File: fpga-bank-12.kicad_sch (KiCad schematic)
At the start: 1 part, among them U4 XC7K160T-FFG676

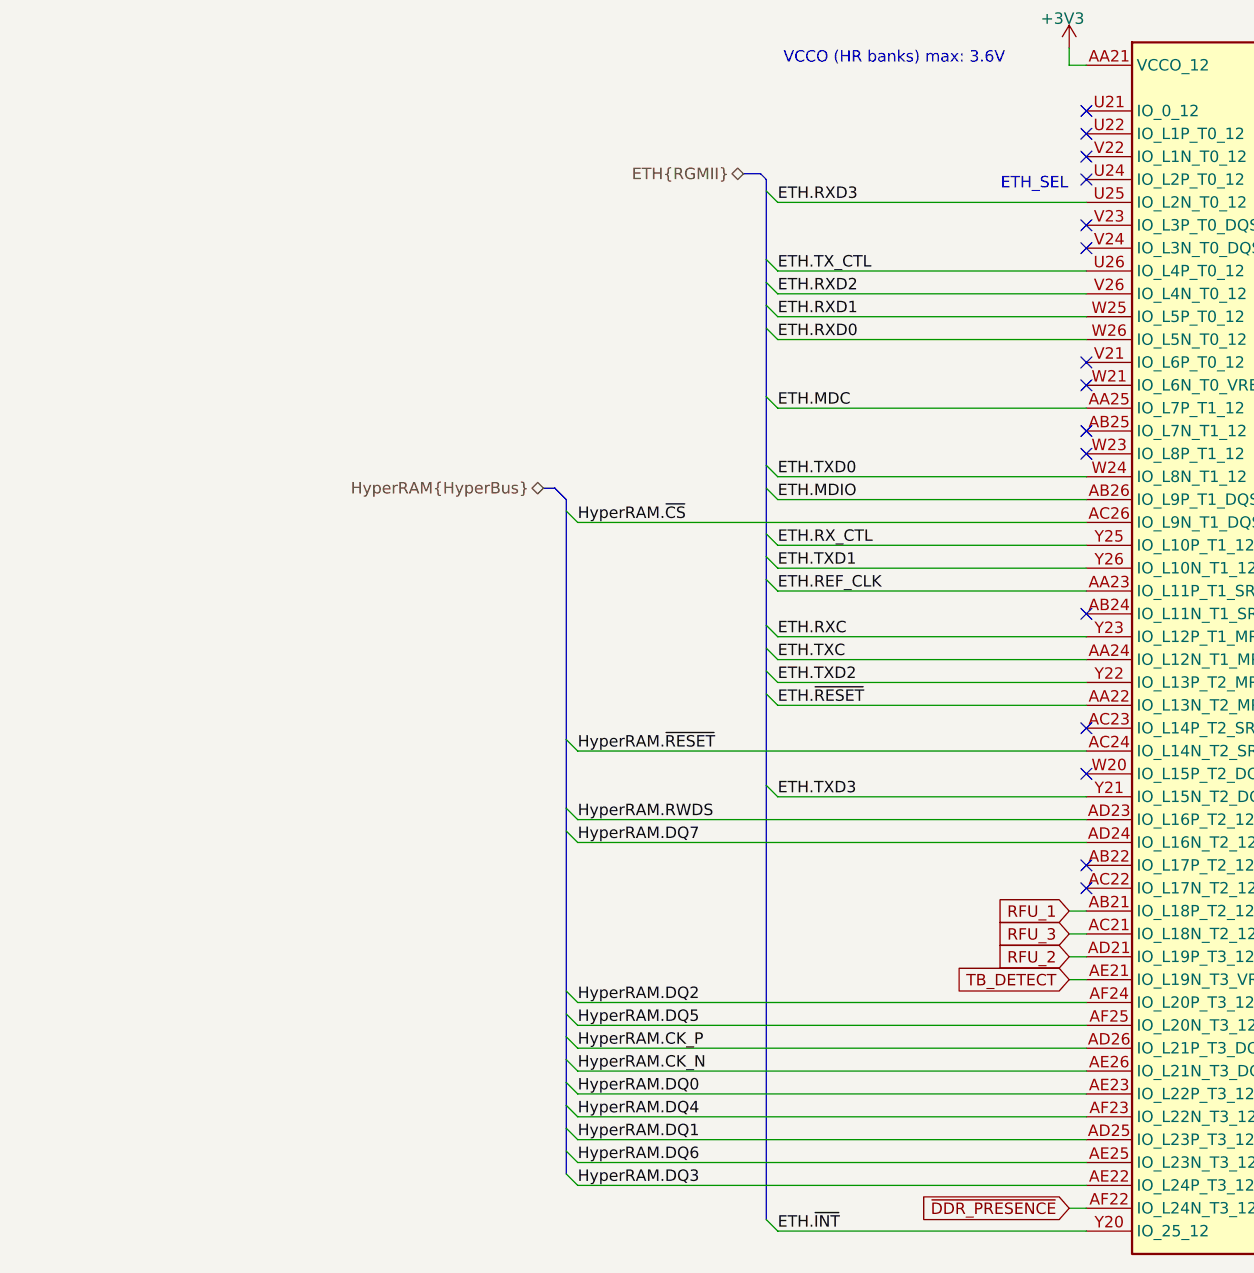
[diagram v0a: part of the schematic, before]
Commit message: [#58418] Update obsolete MPNs. Replace fuses. Remap PWR_EN and PWR_GOOD. Add UART logic level conventers. Bump revision to 1.2.0
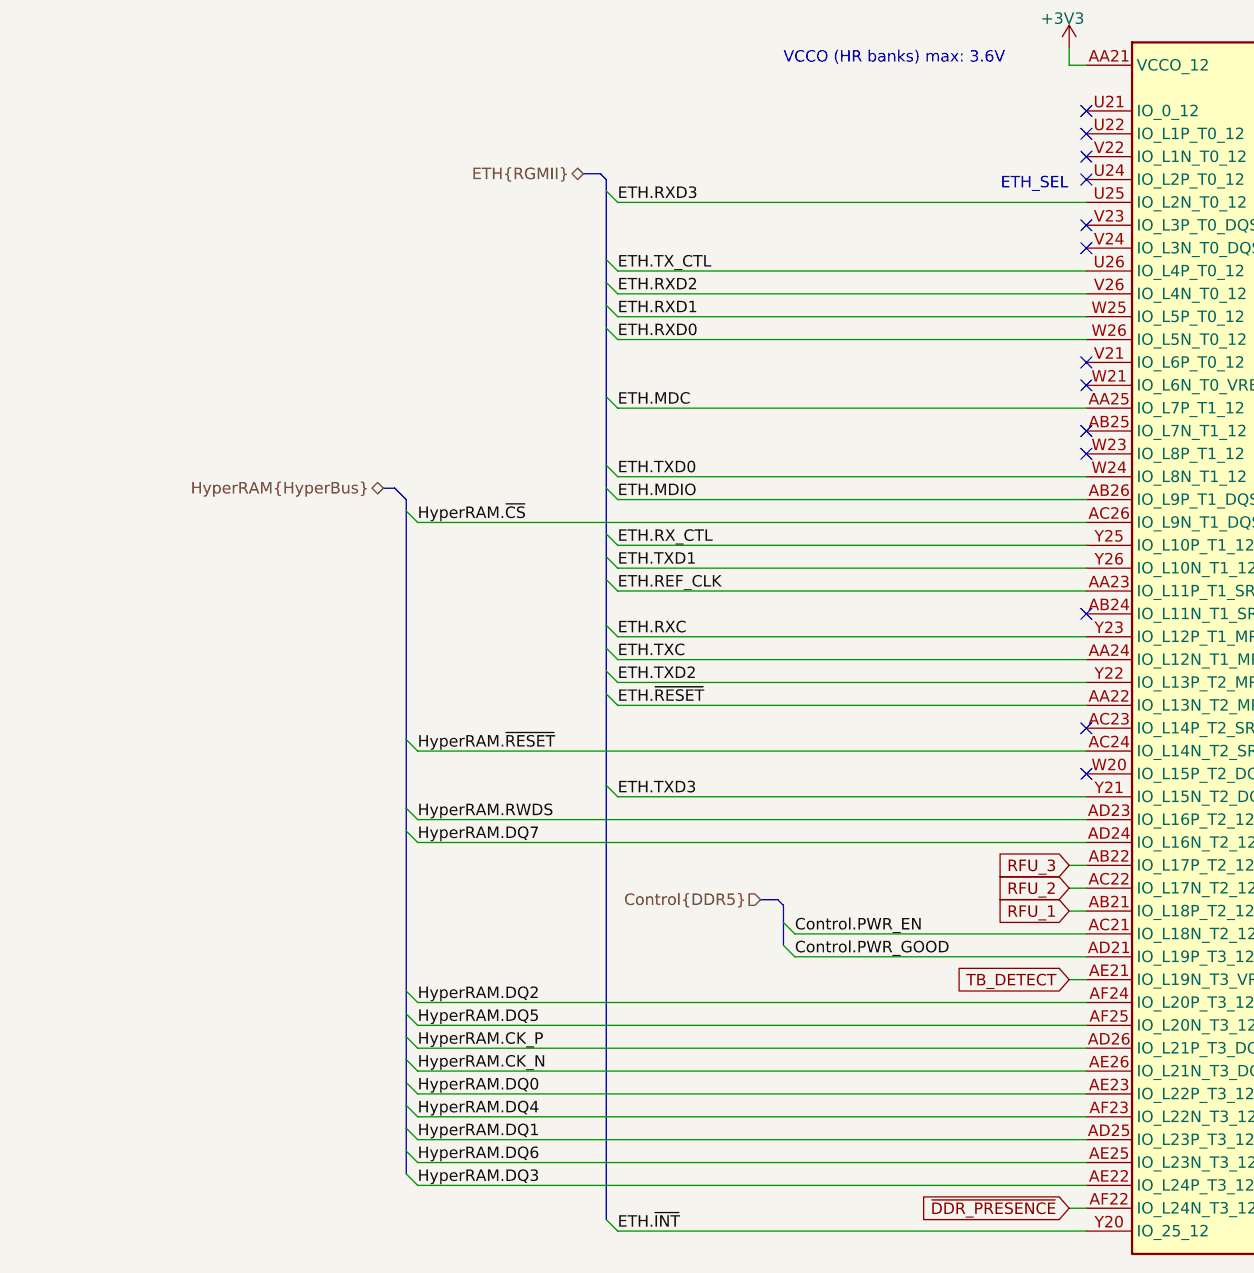
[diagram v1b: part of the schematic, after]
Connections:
- net RFU_2: now also U4.AC22 (IO_L17N_T2_12); no longer U4.AD21 (IO_L19P_T3_12)
- net RFU_3: now also U4.AB22 (IO_L17P_T2_12); no longer U4.AC21 (IO_L18N_T2_12)
- new net Control.PWR_EN: U4.AC21 (IO_L18N_T2_12)
- new net Control.PWR_GOOD: U4.AD21 (IO_L19P_T3_12)
- no-connect marks 15 -> 13

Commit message: [#87036] Add IC testpoints
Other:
- company: (none) -> Antmicro Ltd.
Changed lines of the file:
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@@
 	(title_block
 		(title "SO-DIMM DDR5 Tester")
-		(date "2025-11-25")
+		(date "2025-11-26")
 		(rev "1.3.0")
+		(company "Antmicro Ltd.")
 		(comment 1 "www.antmicro.com")
 		(comment 2 "Antmicro Ltd")
